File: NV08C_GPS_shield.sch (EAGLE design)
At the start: 54 parts, among them IC1 MCP1702-3.3, IC2 74LVC1T45SOT23-HAND, IC3 74LVC1T45SOT23-HAND, IC4 74LVC1T45SOT23-HAND, IC5 74LVC1T45SOT23-HAND, IC6 74LVC1T45SOT23-HAND, IC7 74LVC1T45SOT23-HAND, X1 MEGA2560, X2 CONN-SMATHD-SMD-EDGE, X3 U.FL

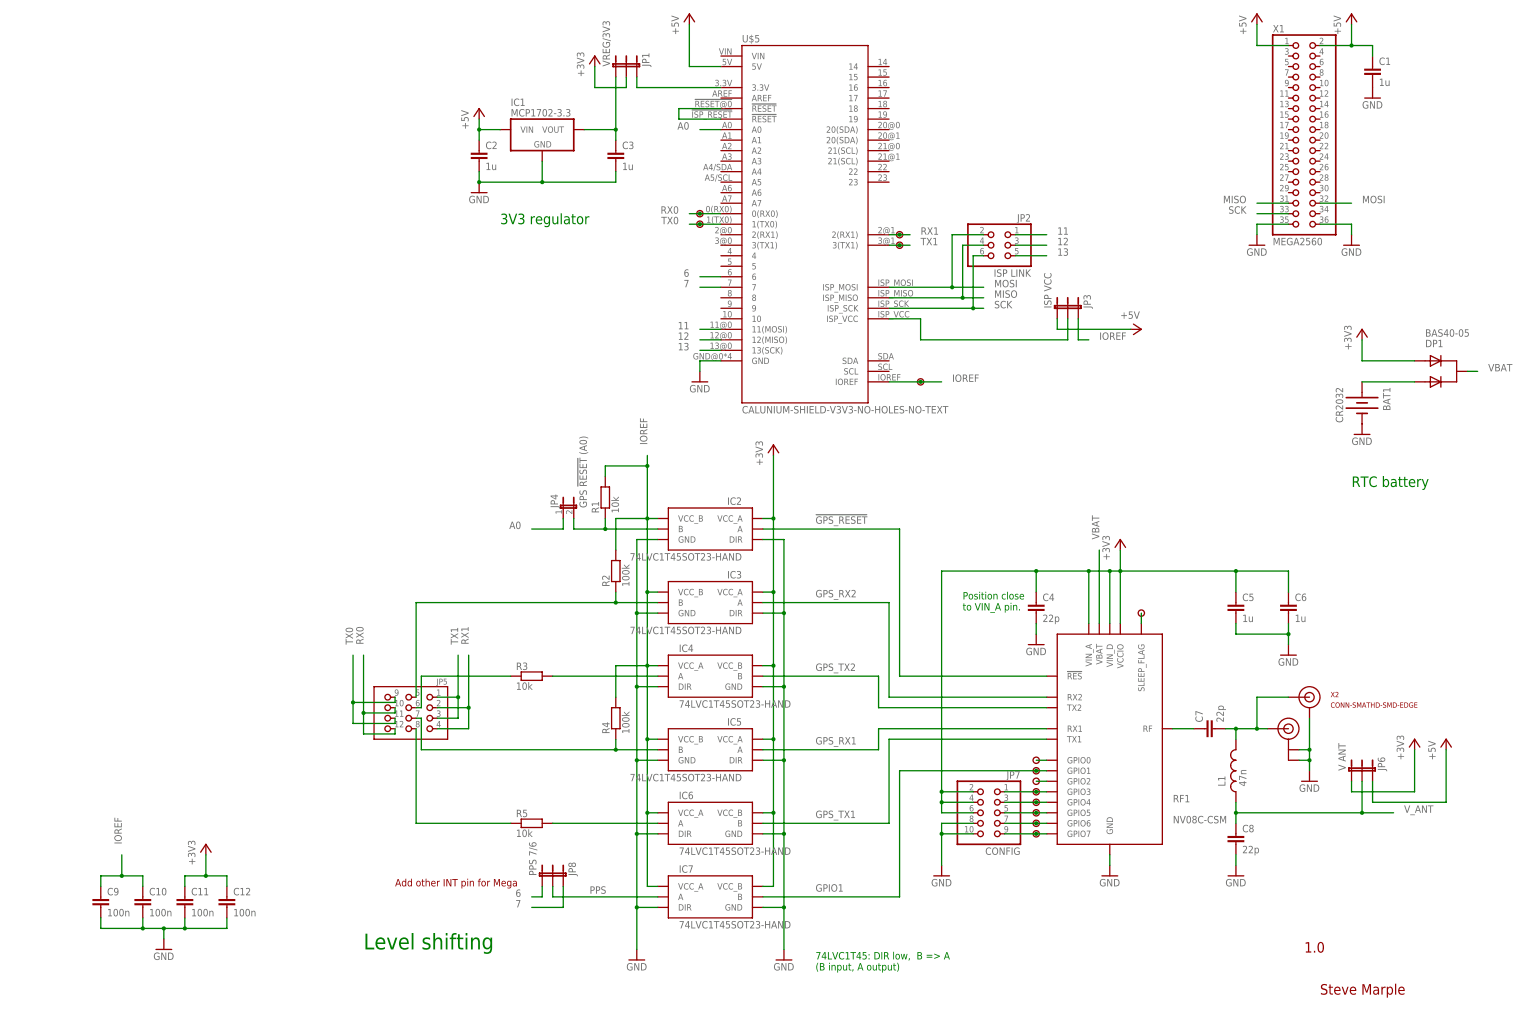
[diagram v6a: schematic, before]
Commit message: Layout and silkscreen changes. Ground pour added.
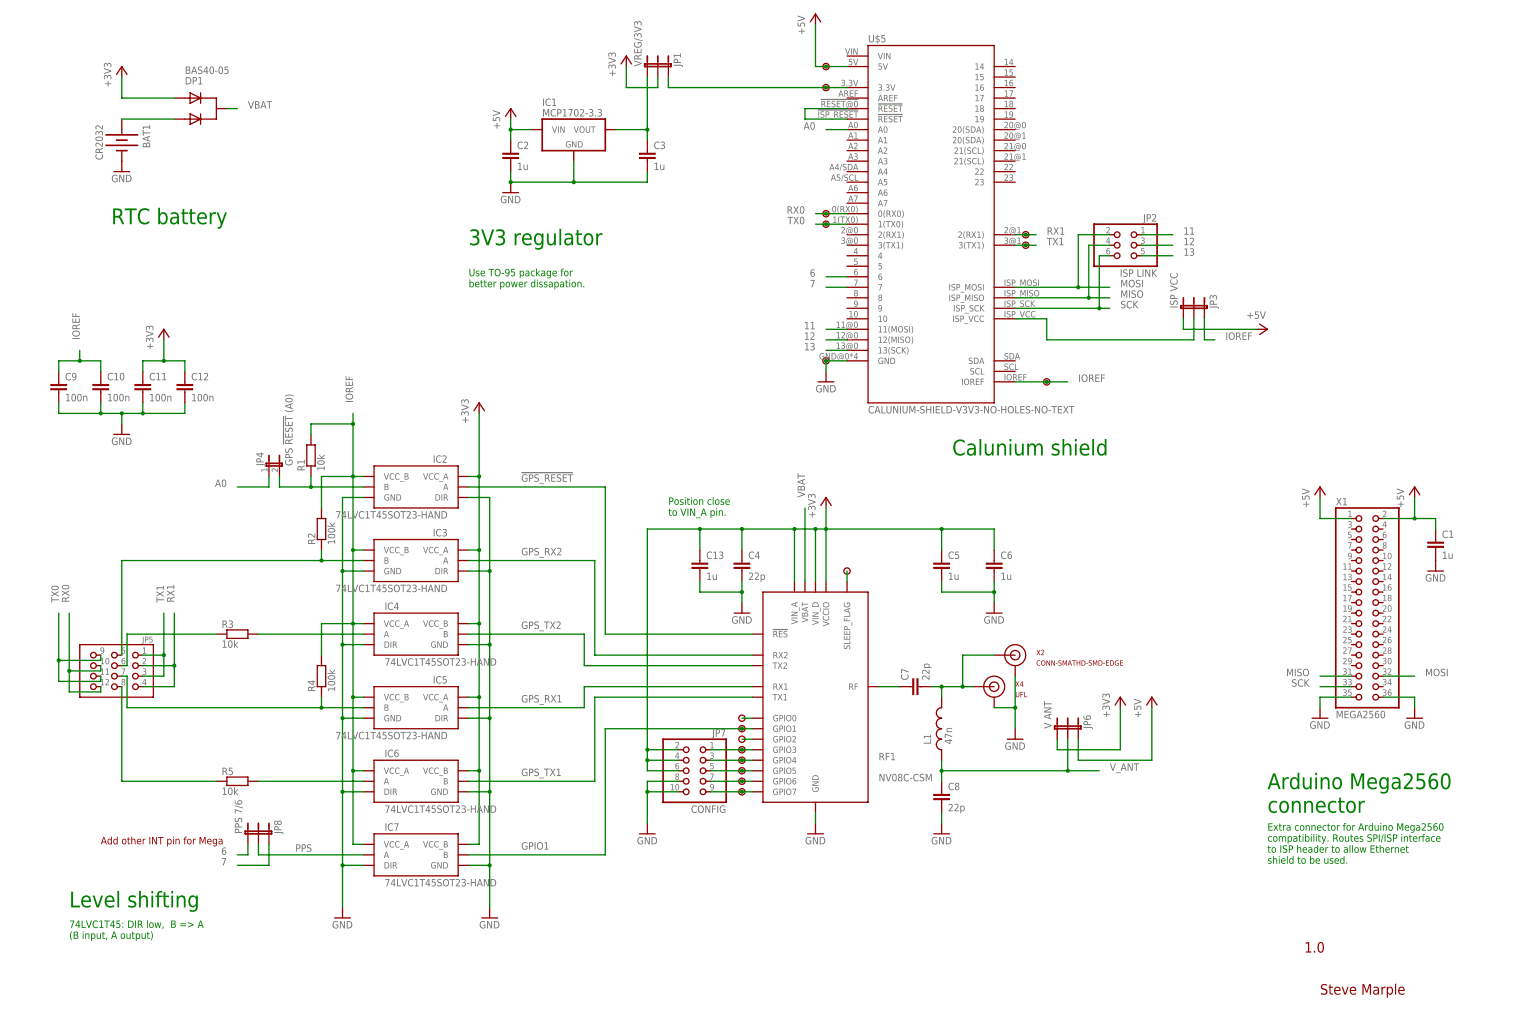
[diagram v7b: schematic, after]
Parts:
- removed X3: U.FL, SparkFun:U.FL
- added C13: 1u, SteveMarple:C-EU1206-HAND
- added U$16, U$17, U$18: PAD, SteveMarple:PAD
- added X4: UFL, SteveMarple:CONN-UFLHAND
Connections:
- net +3V3: now also C13.1
- net +5V: now also U$17.1
- net 3V3_SHIELD: now also U$16.1
- net GND: now also C13.2, U$18.1, X4.GND; no longer X3.GND@0, X3.GND@1
- net N$4: now also X4.SIGNAL; no longer X3.SIGNAL
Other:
- note added: "Arduino Mega2560 connector"
- note added: "Calunium shield"
- note added: "Extra connector for Arduino Mega2560 compatibility. Routes SPI/ISP interface to ISP header to allow Ethernet shield to be used."
- note added: "Use TO-95 package for better power dissapation."
- moved on the sheet: BAT1, C1, C10, C11, C12, C2, C3, C4, C5, C6, C7, C8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
